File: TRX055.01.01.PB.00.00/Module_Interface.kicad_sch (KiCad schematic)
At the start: 3 parts, among them J1 DF40HC-80DS

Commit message: Update Layout
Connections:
- net LS_GPIO7 is gone; now on net HS_DIFF_CLK0_N: J1.21
- net LS_GPIO8 is gone; now on net GND: J1.23
- net LS_GPIO9 is gone; now on net HS_DIFF_1_N: J1.25
- net GND: now also J1.13, J1.17, J1.18, J1.24, J1.33, J1.47, J1.48, J1.61, J1.62, J1.9; no longer J1.12, J1.20, J1.22, J1.27, J1.31, J1.39, J1.40, J1.49, J1.50, J1.59, J1.60, J1.69, J1.70
- net HS_DIFF_0_N: now also J1.26; no longer J1.76
- net HS_DIFF_0_P: now also J1.28; no longer J1.78
- net HS_DIFF_10_N: now also J1.50; no longer J1.65
- net HS_DIFF_10_P: now also J1.52; no longer J1.67
- net HS_DIFF_11_N: now also J1.49; no longer J1.61
- net HS_DIFF_11_P: now also J1.51; no longer J1.63
- net HS_DIFF_12_N: now also J1.54; no longer J1.55
- net HS_DIFF_12_P: now also J1.56; no longer J1.57
- net HS_DIFF_13_N: now also J1.53; no longer J1.51
- net HS_DIFF_13_P: now also J1.55; no longer J1.53
- net HS_DIFF_14_N: now also J1.58; no longer J1.45
- net HS_DIFF_14_P: now also J1.60; no longer J1.47
- net HS_DIFF_15_N: now also J1.57; no longer J1.41
- net HS_DIFF_15_P: now also J1.59; no longer J1.43
- net HS_DIFF_1_N: no longer J1.72
- net HS_DIFF_1_P: now also J1.27; no longer J1.74
- net HS_DIFF_2_N: now also J1.30; no longer J1.66
- net HS_DIFF_2_P: now also J1.32; no longer J1.68
- net HS_DIFF_3_N: now also J1.29; no longer J1.62
- net HS_DIFF_3_P: now also J1.31; no longer J1.64
- net HS_DIFF_4_N: now also J1.36; no longer J1.56
- net HS_DIFF_4_P: now also J1.38; no longer J1.58
- net HS_DIFF_5_N: now also J1.35; no longer J1.52
- net HS_DIFF_5_P: now also J1.37; no longer J1.54
- net HS_DIFF_6_N: now also J1.40; no longer J1.46
- net HS_DIFF_6_P: now also J1.42; no longer J1.48
- net HS_DIFF_7_N: now also J1.39; no longer J1.42
- net HS_DIFF_7_P: now also J1.41; no longer J1.44
- net HS_DIFF_8_N: now also J1.44; no longer J1.75
- net HS_DIFF_8_P: now also J1.46; no longer J1.77
- net HS_DIFF_9_N: now also J1.43; no longer J1.71
- net HS_DIFF_9_P: now also J1.45; no longer J1.73
- net HS_DIFF_CLK0_N: no longer J1.36
- net HS_DIFF_CLK0_P: now also J1.19; no longer J1.38
- net HS_DIFF_CLK1_N: now also J1.22; no longer J1.35
- net HS_DIFF_CLK1_P: now also J1.20; no longer J1.37
- net HS_VREF: now also J1.14; no longer J1.32
- net LS_GPIO0: now also J1.72; no longer J1.7
- net LS_GPIO1: now also J1.74; no longer J1.9
- net LS_GPIO2: now also J1.76; no longer J1.11
- net LS_GPIO3: now also J1.78; no longer J1.13
- net LS_GPIO4: now also J1.63; no longer J1.15
- net LS_GPIO5: now also J1.65; no longer J1.17
- net LS_GPIO6: now also J1.67; no longer J1.19
- net LS_VREF: now also J1.64; no longer J1.30
- net MOD_SPI_MISO: now also J1.68; no longer J1.3
- net MOD_SPI_MOSI: now also J1.70; no longer J1.1
- net MOD_SPI_SCK: now also J1.66; no longer J1.5
- net VDD_1V8D: now also J1.8; no longer J1.28
- net VDD_3V3D: now also J1.5, J1.7; no longer J1.24, J1.26
- net VDD_5V5A: now also J1.1, J1.3; no longer J1.14, J1.16, J1.18
- net VDD_SYSTEM: no longer J1.10, J1.8
- net at R5.1: now also J1.15; no longer J1.33
- net at R1.1: now also J1.11; no longer J1.29
- new net I2C_A0: J1.73
- new net I2C_A1: J1.71
- new net I2C_A2: J1.69
- new net I2C_SCL: J1.77
- new net I2C_SDA: J1.75
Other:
- moved on the sheet: R1, R5

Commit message: +ETH +USB +Connectors
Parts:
- J1: footprint ppa-forms:module_sdr_kit_base -> Resistor_SMD:R_01005_0402Metric
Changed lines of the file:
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@@
 			)
 		)
-		(property "Footprint" "ppa-forms:module_sdr_kit_base"
+		(property "Footprint" "Resistor_SMD:R_01005_0402Metric"
 			(at 136.652 160.274 0)
 			(effects

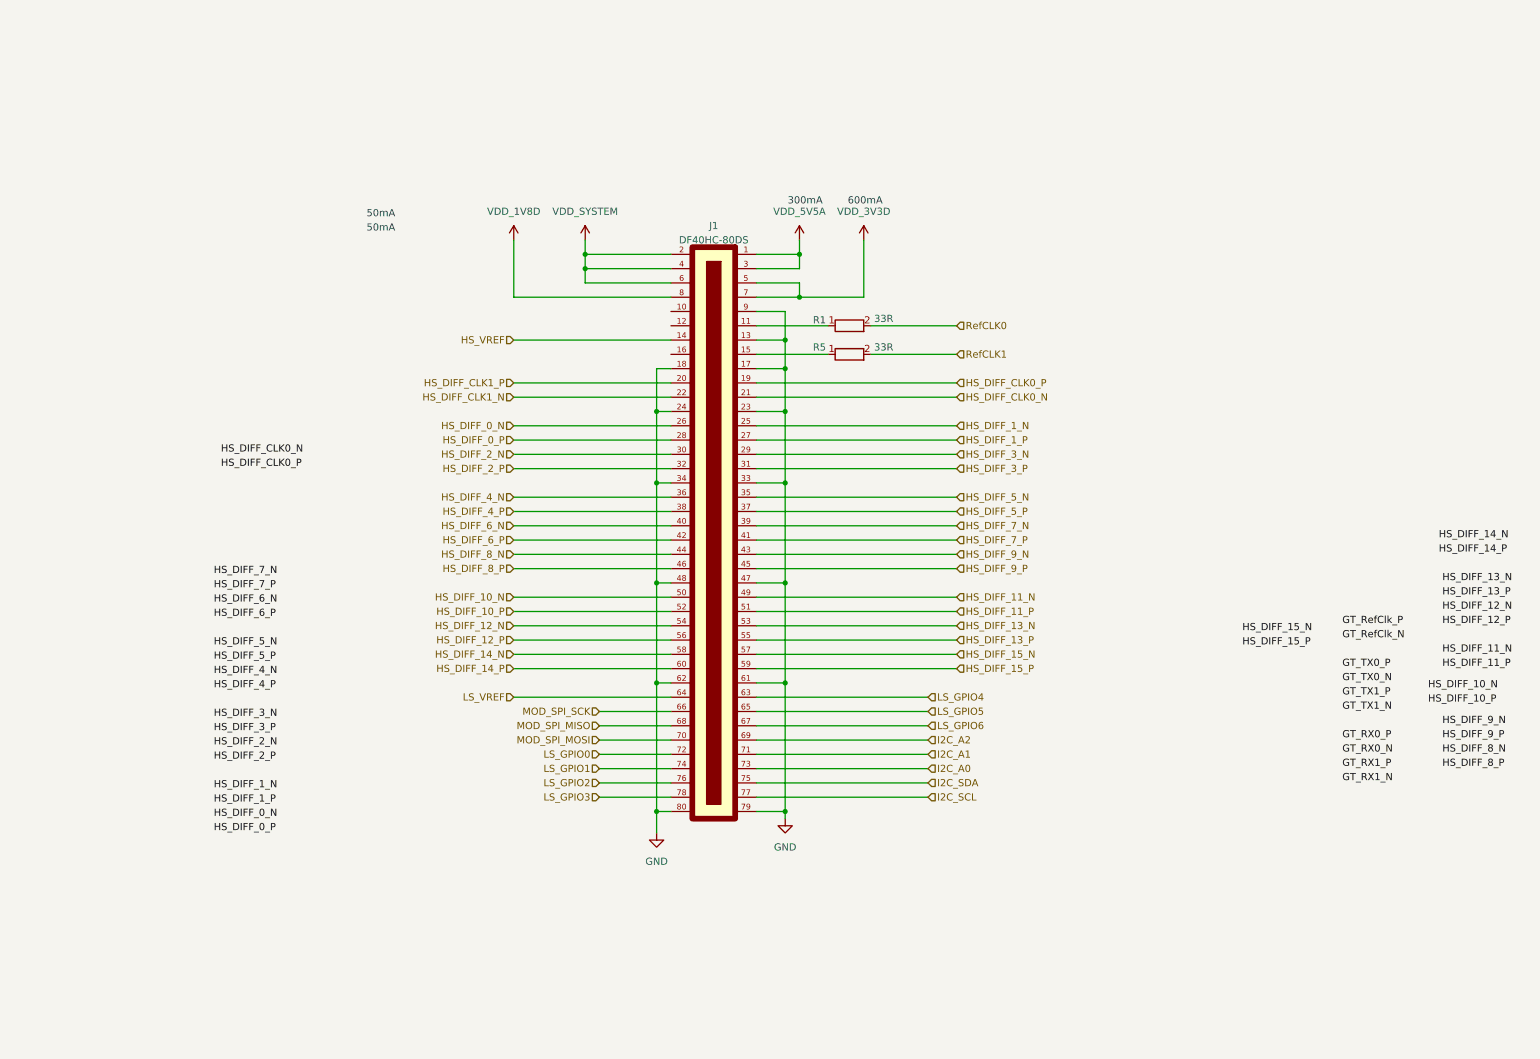
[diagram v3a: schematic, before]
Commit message: + add clocks + add PSU
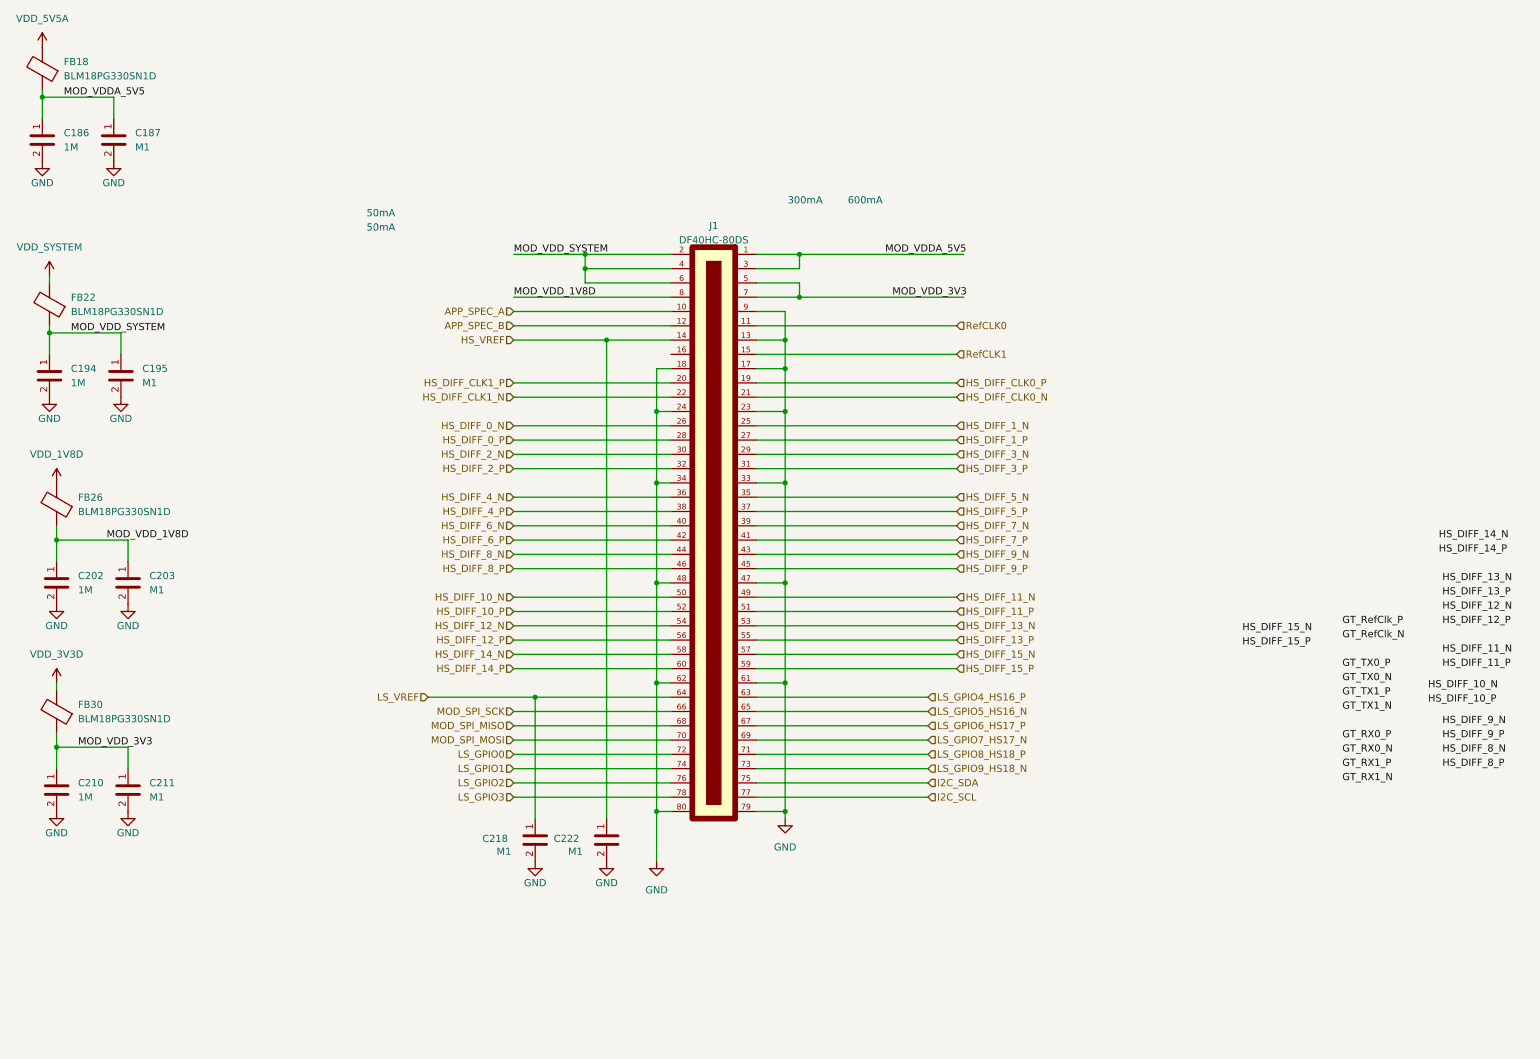
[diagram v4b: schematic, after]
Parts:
- removed R1, R5: 33R, Resistor_SMD:R_0402_1005Metric, symbol PPA-Pasive:Res
- added C186, C194, C202, C210: 1M, Capacitor_SMD:C_0402_1005Metric, symbol PPA-Pasive:Cap
- added C187, C195, C203, C211, C218, C222: M1, Capacitor_SMD:C_0201_0603Metric, symbol PPA-Pasive:Cap
- added FB18, FB22, FB26, FB30: BLM18PG330SN1D, Inductor_SMD:L_0603_1608Metric, symbol Device:FerriteBead
- J1: JLCPCB Part # (none) -> C5254351
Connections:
- net GND: now also C186.2, C187.2, C194.2, C195.2, C202.2, C203.2, C210.2, C211.2, C218.2, C222.2
- net HS_VREF: now also C222.1
- net LS_VREF: now also C218.1
- net RefCLK0: now also J1.11
- net RefCLK1: now also J1.15
- net VDD_1V8D: now also FB26.2; no longer J1.8
- net VDD_3V3D: now also FB30.2; no longer J1.5, J1.7
- net VDD_5V5A: now also FB18.2; no longer J1.1, J1.3
- net VDD_SYSTEM: now also FB22.2; no longer J1.2, J1.4, J1.6
- net APP_SPEC_A: now reaches J1.10
- net APP_SPEC_B: now reaches J1.12
- net I2C_A0 renamed LS_GPIO9_HS18_N
- net I2C_A1 renamed LS_GPIO8_HS18_P
- net I2C_A2 renamed LS_GPIO7_HS17_N
- net LS_GPIO4 renamed LS_GPIO4_HS16_P
- net LS_GPIO5 renamed LS_GPIO5_HS16_N
- net LS_GPIO6 renamed LS_GPIO6_HS17_P
- new net MOD_VDDA_5V5: C186.1, C187.1, FB18.1, J1.1, J1.3
- new net MOD_VDD_1V8D: C202.1, C203.1, FB26.1, J1.8
- new net MOD_VDD_3V3: C210.1, C211.1, FB30.1, J1.5, J1.7
- new net MOD_VDD_SYSTEM: C194.1, C195.1, FB22.1, J1.2, J1.4, J1.6

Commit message: V0.1 - production, added brig-up comments
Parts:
- removed J1: DF40HC-80DS, Resistor_SMD:R_01005_0402Metric, symbol SDR:DF40HC(4.0)-80DS-0.4V_51_KA
- added M1: DF40HC-80DS, ppa-forms:module_sdr_kit_base, symbol SDR_Tronex:SDR_MOD_DF40HC-80DS
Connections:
- net APP_SPEC_A: now also M1.10
- net APP_SPEC_B: now also M1.12
- net GND: now also M1.13, M1.17, M1.18, M1.23, M1.24, M1.33, M1.34, M1.47, M1.48, M1.61, M1.62, M1.79, M1.80, M1.9, M1.SH0, M1.SH1
- net HS_DIFF_0_N: now also M1.26
- net HS_DIFF_0_P: now also M1.28
- net HS_DIFF_10_N: now also M1.50
- net HS_DIFF_10_P: now also M1.52
- net HS_DIFF_11_N: now also M1.49
- net HS_DIFF_11_P: now also M1.51
- net HS_DIFF_12_N: now also M1.54
- net HS_DIFF_12_P: now also M1.56
- net HS_DIFF_13_N: now also M1.53
- net HS_DIFF_13_P: now also M1.55
- net HS_DIFF_14_N: now also M1.58
- net HS_DIFF_14_P: now also M1.60
- net HS_DIFF_15_N: now also M1.57
- net HS_DIFF_15_P: now also M1.59
- net HS_DIFF_1_N: now also M1.25
- net HS_DIFF_1_P: now also M1.27
- net HS_DIFF_2_N: now also M1.30
- net HS_DIFF_2_P: now also M1.32
- net HS_DIFF_3_N: now also M1.29
- net HS_DIFF_3_P: now also M1.31
- net HS_DIFF_4_N: now also M1.36
- net HS_DIFF_4_P: now also M1.38
- net HS_DIFF_5_N: now also M1.35
- net HS_DIFF_5_P: now also M1.37
- net HS_DIFF_6_N: now also M1.40
- net HS_DIFF_6_P: now also M1.42
- net HS_DIFF_7_N: now also M1.39
- net HS_DIFF_7_P: now also M1.41
- net HS_DIFF_8_N: now also M1.44
- net HS_DIFF_8_P: now also M1.46
- net HS_DIFF_9_N: now also M1.43
- net HS_DIFF_9_P: now also M1.45
- net HS_DIFF_CLK0_N: now also M1.21
- net HS_DIFF_CLK0_P: now also M1.19
- net HS_DIFF_CLK1_N: now also M1.22
- net HS_DIFF_CLK1_P: now also M1.20
- net HS_VREF: now also M1.14
- net I2C_SCL: now also M1.77
- net I2C_SDA: now also M1.75
- net LS_GPIO0: now also M1.72
- net LS_GPIO1: now also M1.74
- net LS_GPIO2: now also M1.76
- net LS_GPIO3: now also M1.78
- net LS_GPIO4_HS16_P: now also M1.63
- net LS_GPIO5_HS16_N: now also M1.65
- net LS_GPIO6_HS17_P: now also M1.67
- net LS_GPIO7_HS17_N: now also M1.69
- net LS_GPIO8_HS18_P: now also M1.71
- net LS_GPIO9_HS18_N: now also M1.73
- net LS_VREF: now also M1.64
- net MOD_SPI_MISO: now also M1.68
- net MOD_SPI_MOSI: now also M1.70
- net MOD_SPI_SCK: now also M1.66
- net MOD_VDDA_5V5: now also M1.1, M1.3
- net MOD_VDD_1V8D: now also M1.8
- net MOD_VDD_3V3: now also M1.5, M1.7
- net MOD_VDD_SYSTEM: now also M1.2, M1.4, M1.6
- net RefCLK0: now also M1.11
- net RefCLK1: now also M1.15
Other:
- note added: "DF40HC: 300mA@pin"
- company: (none) -> Tronex s.r.o. / Tronex Group USA LLC
- title: (none) -> TRNX SDR Carrier board
- moved on the sheet: C186, C187, C194, C195, C202, C203, C210, C211, C218, C222, FB18, FB22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
